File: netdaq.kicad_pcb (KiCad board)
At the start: 2 copper layers, 131.5 x 93 mm, 289 parts, among them J1 RJ45, J3 Conn_01x06_Pin, J4 Micro_SD_Card_Det2, U1 PIC32CK1025GC01100-I/4SB, U10 TLA2518IRTER, U11 TLA2518IRTER, U2 LAN8720A-CP, U5 MP6004GQ-P, U6 PD70100ILD-TR, U7 TPS62A01PDDCR, U8 TLA2518IRTER, U9 TLA2518IRTER, Y4 Crystal_GND24

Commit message: lots
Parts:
- removed TR2: Wuerth_750343373, Transformer_THT:Transformer_Wuerth_750343373
- added C102: 910p, Capacitor_SMD:C_0402_1005Metric, F.Cu at (183.6, 68.5)
- added C103: 22u 10 V, Capacitor_SMD:C_0805_2012Metric, F.Cu at (178.8, 87.2)
- added C104: 22u 10 V, Capacitor_SMD:C_0805_2012Metric, F.Cu at (176.2, 87.2)
- added C105: 220u, Capacitor_SMD:C_Elec_6.3x7.7, F.Cu at (171.2, 87.2)
- added C106: 2.2u 100 V, Capacitor_SMD:C_1206_3216Metric, F.Cu at (180.6, 59.2)
- added C107: 1u 10V, Capacitor_SMD:C_0402_1005Metric, F.Cu at (177.6, 64.0)
- added C108: C, Capacitor_SMD:C_0402_1005Metric, F.Cu at (185.2, 82.8)
- added C134: 47u, Capacitor_SMD:C_Elec_10x10.2, F.Cu at (171.2, 63.8)
- added C135: 100n 100V, Capacitor_SMD:C_0603_1608Metric, F.Cu at (165.5, 72.3)
- added C136: 4.7u, Capacitor_SMD:C_0805_2012Metric, F.Cu at (168.0, 70.2)
- added D37: US1MFA, Diode_SMD:D_SOD-123F, F.Cu at (180.8, 68.2)
- added D38: VS-10BQ060-M3/5BT, SMB:SMB(DO-214AA), F.Cu at (182.0, 86.2)
- added D39: SMBJ58A, Diode_SMD:D_SMB, F.Cu at (161.0, 60.5)
- added D80: MMBZ5256ELT1G, MMBZ5256ELT1G:SOT-23(1-3), F.Cu at (184.1, 61.2)
- added FB4: FerriteBead, Resistor_SMD:R_0402_1005Metric, F.Cu at (203.3, 76.0)
- added H1: MountingHole, MountingHole:MountingHole_3.2mm_M3_ISO14580, F.Cu at (133.5, 60.0)
- added H2: MountingHole, MountingHole:MountingHole_3.2mm_M3_ISO14580, F.Cu at (206.5, 60.0)
- added H3: MountingHole, MountingHole:MountingHole_3.2mm_M3_ISO14580, F.Cu at (133.5, 135.5)
- added H4: MountingHole, MountingHole:MountingHole_3.2mm_M3_ISO14580, F.Cu at (206.5, 135.5)
- added R100: 240k, Resistor_SMD:R_0402_1005Metric, F.Cu at (172.8, 75.0)
- added R101: 133, Resistor_SMD:R_0402_1005Metric, F.Cu at (172.8, 73.8)
- added R102: 24.9k, Resistor_SMD:R_0402_1005Metric, F.Cu at (165.2, 75.2)
- added R103: 500, Resistor_SMD:R_0603_1608Metric, F.Cu at (185.2, 87.5)
- added R104: 13k, Resistor_SMD:R_0402_1005Metric, F.Cu at (184.1, 65.0)
- added R105: 10k, Resistor_SMD:R_0402_1005Metric, F.Cu at (184.1, 63.7)
- added R106: 330k, Resistor_SMD:R_0402_1005Metric, F.Cu at (177.6, 62.0)
- added R76: 56k, Resistor_SMD:R_0402_1005Metric, F.Cu at (183.6, 66.5)
- added R77: R, Resistor_SMD:R_0402_1005Metric, F.Cu at (185.2, 84.8)
- added R78: 68k, Resistor_SMD:R_0402_1005Metric, F.Cu at (177.6, 68.0)
- added R79: 12k, Resistor_SMD:R_0402_1005Metric, F.Cu at (177.6, 66.0)
- added T2: POE30P-50L, POE30P-50L:POE30P-50L, F.Cu at (179.5, 76.5)
- added U12: PD70100ILD-TR, PD70100ILD-TR:DFN12_4X3_MCH, F.Cu at (169.0, 73.6)
- added USB1: HYCW498-USBC16-735B, C42400252:USB-C-SMD_HYCW498-USBC16-735B, F.Cu at (197.0, 60.0)
- U6: value PD70100ILD-TR -> TPUSBLC6-4SC6; footprint PD70100ILD-TR:DFN12_4X3_MCH -> Package_TO_SOT_SMD:SOT-23-6_Handsoldering
- moved J3 163.1 mm to (205.0, 115.4)
- moved C109 109.4 mm to (192.0, 88.5), turned to 0 degrees
- moved R81 105.6 mm to (188.5, 89.5), turned to 180 degrees
- moved U7 103.1 mm to (190.0, 92.5), turned to 90 degrees
- moved L1 102.8 mm to (194.0, 95.5), turned to -90 degrees
- moved R83 102.5 mm to (187.5, 91.5), turned to 90 degrees
- moved R80 101.4 mm to (186.0, 91.5), turned to -90 degrees
- moved R82 98.2 mm to (187.5, 95.0), turned to -90 degrees
- moved C110 95.8 mm to (190.4, 99.0), turned to 180 degrees
- moved C112 92.9 mm to (190.4, 101.5), turned to 180 degrees
- moved C111 90.1 mm to (190.4, 104.0), turned to 180 degrees
- moved U6 25.9 mm to (198.9, 77.5)
- moved U3 7.64 mm to (160.5, 65.6)
- moved U4 7.63 mm to (160.5, 72.3)
- moved U5 5.52 mm to (180.5, 64.0), turned to 180 degrees
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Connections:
- U5 pad 1: ETH_SHIELD -> PGND
- U5 pad 10: ETH_SHIELD -> PGND
- U5 pad 15: ETH_SHIELD -> PGND
- U5 pad 2: ETH_SHIELD -> PGND
- U5 pad 3: unconnected-(U5-EN-Pad3) -> /PoE Regulator/FLY_EN
- U5 pad 5: /PoE Regulator/VIN -> /Ethernet Connector/POE_V+
- U5 pad 6: /PoE Regulator/VIN -> /Ethernet Connector/POE_V+
- U5 pad 7: unconnected-(U5-MODE-Pad7) -> PGND
- U5 pad 9: unconnected-(U5-ILIM-Pad9) -> Net-(U5-ILIM)
- U6 pad 1: unconnected-(U6-RDET-Pad1) -> /USB.D+
- U6 pad 2: unconnected-(U6-RREF-Pad2) -> GND
- U6 pad 5: unconnected-(U6-VPNIN-Pad5) -> /USB Connector/EXT_VBUS
- U6 pad 6: unconnected-(U6-NC-Pad6) -> /USB.D-
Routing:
- net /Ethernet Connector/POE_V-: track 0.00 -> 27.2 mm
- net PGND: track 0.00 -> 20.2 mm
- net /RMII.TXD1: track 27.6 -> 13.8 mm
- net /RMII.TXD0: track 27.2 -> 14.5 mm
- net /SMI.MDIO: track 47.7 -> 35.5 mm
- net /RMII.TXEN: track 26.9 -> 14.8 mm
- net /SMI.MDC: track 47.8 -> 36.1 mm
- net /RMII.CRSDV: track 26.7 -> 15.1 mm
- net /Ethernet Connector/POE_V+: track 0.00 -> 10.5 mm, vias 0 -> 16
- net /RMII.RXER: track 34.3 -> 24.3 mm
- net +5.0V: track 0.91 -> 8.01 mm
- net /RMII.RXD1: track 43.4 -> 36.5 mm
- net /PoE Regulator/FLY_SW: track 0.00 -> 6.70 mm
- net GND: track 12.2 -> 18.8 mm
- net /PoE Regulator/FLY_FB: track 0.00 -> 6.29 mm, vias 0 -> 2
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- added copper zone on F.Cu, net /Ethernet Connector/POE_CT1
- added copper zone on F.Cu, net /Ethernet Connector/POE_CT2
- added copper zone on B.Cu, net /Ethernet Connector/POE_V+
- added copper zone on F.Cu, net /Ethernet Connector/POE_V+
- added copper zone on F.Cu, net /Ethernet Connector/POE_V-
- added copper zone on F.Cu, net /PD Controller/PD_AUX
- added copper zone on F.Cu, net /PoE Regulator/FLY_SW
- added copper zone on F.Cu, net Net-(D38-A)
- added copper zone on F.Cu, net Net-(R33-Pad1)
- added copper zone on F.Cu, net Net-(R34-Pad1)
- added copper zone on F.Cu, net PGND
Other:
- board size 131.5 x 93 mm -> 80 x 89 mm
- board text removed: "3v3"

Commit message: almost finished usb
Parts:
- added C127: 100n 10V, Capacitor_SMD:C_0402_1005Metric, F.Cu at (194.2, 72.8)
- added C128: 10u 10V, Capacitor_SMD:C_0805_2012Metric, F.Cu at (194.0, 74.5)
- added R92: 5.1k, Resistor_SMD:R_0402_1005Metric, F.Cu at (198.5, 65.5)
- added R93: 5.1k, Resistor_SMD:R_0402_1005Metric, F.Cu at (195.5, 65.5)
- added TP172: TestPoint, TestPoint:TestPoint_THTPad_D1.0mm_Drill0.5mm, F.Cu at (193.0, 67.5)
- added TP173: TestPoint, TestPoint:TestPoint_THTPad_D1.0mm_Drill0.5mm, F.Cu at (204.0, 70.5)
- added TP174: TestPoint, TestPoint:TestPoint_THTPad_D1.0mm_Drill0.5mm, F.Cu at (204.0, 73.0)
- added TP175: TestPoint, TestPoint:TestPoint_THTPad_D1.0mm_Drill0.5mm, F.Cu at (198.5, 71.0)
- added TP176: TestPoint, TestPoint:TestPoint_THTPad_D1.0mm_Drill0.5mm, F.Cu at (195.5, 71.0)
- added TP177: TestPoint_Alt, TestPoint:TestPoint_THTPad_1.0x1.0mm_Drill0.5mm, F.Cu at (201.5, 65.5)
- added TP178: TestPoint, TestPoint:TestPoint_THTPad_D1.0mm_Drill0.5mm, F.Cu at (206.8, 64.5)
- added TP179: TestPoint, TestPoint:TestPoint_THTPad_D1.0mm_Drill0.5mm, F.Cu at (206.8, 66.8)
- added U13: DLM0NSN500HY2D, C913480:FILTER-SMD_4P-L0.8-W0.6-TL_DLP0NSC280HL2L, F.Cu at (197.0, 73.5)
- moved FB4 11.9 mm to (193.0, 70.0), turned to 90 degrees
- moved U6 9.64 mm to (197.0, 68.0), turned to 180 degrees
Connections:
- FB4 pad 1: /USB Connector/VBUS -> +5V_USB
- U6 pad 1: /USB.D+ -> /USB Connector/EXT_USB_D+
- U6 pad 3: unconnected-(U6-Pad3) -> /USB Connector/EXT_USB_CC1
- U6 pad 4: unconnected-(U6-Pad4) -> /USB Connector/EXT_USB_CC2
- U6 pad 6: /USB.D- -> /USB Connector/EXT_USB_D-
- USB1 pad 1: unconnected-(USB1-SHELL-Pad1) -> GND
- USB1 pad 2: (no net) -> GND
- USB1 pad 3: (no net) -> GND
- USB1 pad 4: (no net) -> GND
- USB1 pad A1B12: unconnected-(USB1-GND-PadA1B12) -> GND
- USB1 pad A4B9: unconnected-(USB1-VBUS-PadA4B9) -> /USB Connector/EXT_VBUS
- USB1 pad A5: unconnected-(USB1-CC1-PadA5) -> /USB Connector/EXT_USB_CC1
- USB1 pad A6: unconnected-(USB1-DP1-PadA6) -> /USB Connector/EXT_USB_D+
- USB1 pad A7: unconnected-(USB1-DN1-PadA7) -> /USB Connector/EXT_USB_D-
- USB1 pad A8: unconnected-(USB1-SBU1-PadA8) -> /USB Connector/NC_USB_SBU1
- USB1 pad B1A12: unconnected-(USB1-GND-PadB1A12) -> GND
- USB1 pad B4A9: unconnected-(USB1-VBUS-PadB4A9) -> /USB Connector/EXT_VBUS
- USB1 pad B5: unconnected-(USB1-CC2-PadB5) -> /USB Connector/EXT_USB_CC2
- USB1 pad B6: unconnected-(USB1-DP2-PadB6) -> /USB Connector/EXT_USB_D+
- USB1 pad B7: unconnected-(USB1-DN2-PadB7) -> /USB Connector/EXT_USB_D-
- USB1 pad B8: unconnected-(USB1-SBU2-PadB8) -> /USB Connector/NC_USB_SBU2
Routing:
- net /USB Connector/NC_USB_SBU1: track 0.00 -> 13.6 mm, vias 0 -> 1
- net /USB Connector/NC_USB_SBU2: track 0.00 -> 11.2 mm, vias 0 -> 1
- net /USB Connector/EXT_USB_CC2: track 0.00 -> 5.01 mm
- net /USB Connector/EXT_USB_CC1: track 0.00 -> 4.81 mm
- net GND: track 18.8 -> 21.8 mm

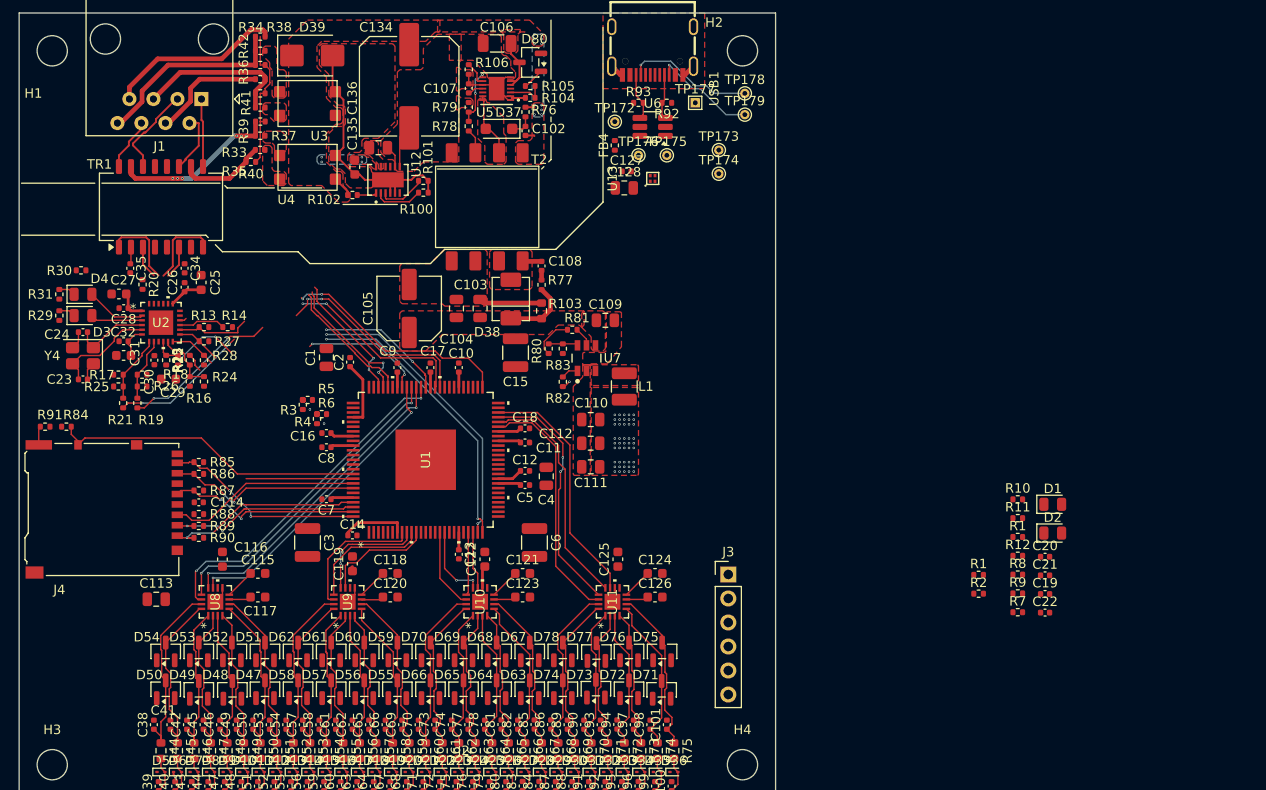
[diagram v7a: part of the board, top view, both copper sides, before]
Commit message: changed to 4 layer, finished usb conn, added jtag conn, some other things
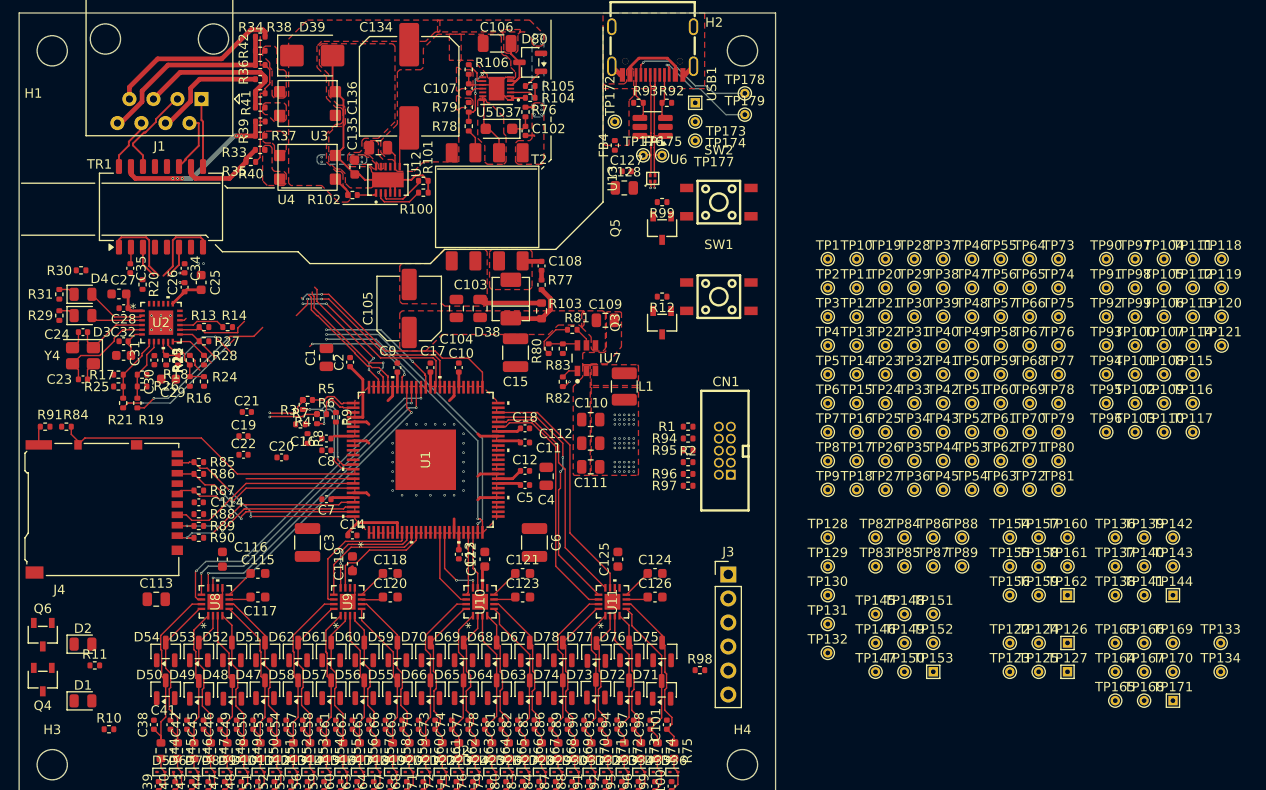
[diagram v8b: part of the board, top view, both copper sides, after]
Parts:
- removed the R1 at (235.6, 111.4)
- added CN1: HX JN1.27-2X5P ZZ H4.9, C42372547:CONN-TH_10P-P1.27_HX-JN1.27-2X5P-ZZ-H4.9, F.Cu at (204.6, 102.3)
- added Q3: BSS138LT1G, C82045:SOT-23-3_L2.9-W1.6-P1.90-LS2.8-BR, F.Cu at (198.0, 88.8)
- added Q4: BSS138LT1G, C82045:SOT-23-3_L2.9-W1.6-P1.90-LS2.8-BR, F.Cu at (132.5, 126.5)
- added Q5: BSS138LT1G, C82045:SOT-23-3_L2.9-W1.6-P1.90-LS2.8-BR, F.Cu at (198.0, 78.8)
- added Q6: BSS138LT1G, C82045:SOT-23-3_L2.9-W1.6-P1.90-LS2.8-BR, F.Cu at (132.5, 121.8)
- added R94: 10k, Resistor_SMD:R_0402_1005Metric, F.Cu at (200.8, 101.0)
- added R95: 10k, Resistor_SMD:R_0402_1005Metric, F.Cu at (200.8, 102.2)
- added R96: 10k, Resistor_SMD:R_0402_1005Metric, F.Cu at (200.8, 104.8)
- added R97: 10k, Resistor_SMD:R_0402_1005Metric, F.Cu at (200.8, 106.0)
- added R98: 10k, Resistor_SMD:R_0402_1005Metric, F.Cu at (202.0, 125.5)
- added R99: 10k, Resistor_SMD:R_0402_1005Metric, F.Cu at (198.0, 76.0)
- added SW1: TS110926043, C22375349:SW-SMD_4P-L4.5-W4.5-P3.00-LS7.5, F.Cu at (204.0, 86.0)
- added SW2: TS110926043, C22375349:SW-SMD_4P-L4.5-W4.5-P3.00-LS7.5, F.Cu at (204.0, 76.0)
- added TP1: TestPoint, TestPoint:TestPoint_THTPad_D1.0mm_Drill0.5mm, F.Cu at (215.5, 82.0)
- added TP10: TestPoint, TestPoint:TestPoint_THTPad_D1.0mm_Drill0.5mm, F.Cu at (218.6, 82.0)
- added TP100: TestPoint, TestPoint:TestPoint_THTPad_D1.0mm_Drill0.5mm, F.Cu at (248.0, 91.2)
- added TP101: TestPoint, TestPoint:TestPoint_THTPad_D1.0mm_Drill0.5mm, F.Cu at (248.0, 94.2)
- added TP102: TestPoint, TestPoint:TestPoint_THTPad_D1.0mm_Drill0.5mm, F.Cu at (248.0, 97.3)
- added TP103: TestPoint, TestPoint:TestPoint_THTPad_D1.0mm_Drill0.5mm, F.Cu at (248.0, 100.3)
- added TP104: TestPoint, TestPoint:TestPoint_THTPad_D1.0mm_Drill0.5mm, F.Cu at (251.1, 82.0)
- added TP105: TestPoint, TestPoint:TestPoint_THTPad_D1.0mm_Drill0.5mm, F.Cu at (251.1, 85.1)
- added TP106: TestPoint, TestPoint:TestPoint_THTPad_D1.0mm_Drill0.5mm, F.Cu at (251.1, 88.1)
- added TP107: TestPoint, TestPoint:TestPoint_THTPad_D1.0mm_Drill0.5mm, F.Cu at (251.1, 91.2)
- added TP108: TestPoint, TestPoint:TestPoint_THTPad_D1.0mm_Drill0.5mm, F.Cu at (251.1, 94.2)
- added TP109: TestPoint, TestPoint:TestPoint_THTPad_D1.0mm_Drill0.5mm, F.Cu at (251.1, 97.3)
- added TP11: TestPoint, TestPoint:TestPoint_THTPad_D1.0mm_Drill0.5mm, F.Cu at (218.6, 85.1)
- added TP110: TestPoint, TestPoint:TestPoint_THTPad_D1.0mm_Drill0.5mm, F.Cu at (251.1, 100.3)
- added TP111: TestPoint, TestPoint:TestPoint_THTPad_D1.0mm_Drill0.5mm, F.Cu at (254.1, 82.0)
- added TP112: TestPoint, TestPoint:TestPoint_THTPad_D1.0mm_Drill0.5mm, F.Cu at (254.1, 85.1)
- added TP113: TestPoint, TestPoint:TestPoint_THTPad_D1.0mm_Drill0.5mm, F.Cu at (254.1, 88.1)
- added TP114: TestPoint, TestPoint:TestPoint_THTPad_D1.0mm_Drill0.5mm, F.Cu at (254.1, 91.2)
- added TP115: TestPoint, TestPoint:TestPoint_THTPad_D1.0mm_Drill0.5mm, F.Cu at (254.1, 94.2)
- added TP116: TestPoint, TestPoint:TestPoint_THTPad_D1.0mm_Drill0.5mm, F.Cu at (254.1, 97.3)
- added TP117: TestPoint, TestPoint:TestPoint_THTPad_D1.0mm_Drill0.5mm, F.Cu at (254.1, 100.3)
- added TP118: TestPoint, TestPoint:TestPoint_THTPad_D1.0mm_Drill0.5mm, F.Cu at (257.2, 82.0)
- added TP119: TestPoint, TestPoint:TestPoint_THTPad_D1.0mm_Drill0.5mm, F.Cu at (257.2, 85.1)
- added TP12: TestPoint, TestPoint:TestPoint_THTPad_D1.0mm_Drill0.5mm, F.Cu at (218.6, 88.1)
- added TP120: TestPoint, TestPoint:TestPoint_THTPad_D1.0mm_Drill0.5mm, F.Cu at (257.2, 88.1)
- added TP121: TestPoint, TestPoint:TestPoint_THTPad_D1.0mm_Drill0.5mm, F.Cu at (257.2, 91.2)
- added TP122: TestPoint, TestPoint:TestPoint_THTPad_D1.0mm_Drill0.5mm, F.Cu at (234.8, 122.6)
- added TP123: TestPoint, TestPoint:TestPoint_THTPad_D1.0mm_Drill0.5mm, F.Cu at (234.8, 125.7)
- added TP124: TestPoint, TestPoint:TestPoint_THTPad_D1.0mm_Drill0.5mm, F.Cu at (237.8, 122.6)
- added TP125: TestPoint, TestPoint:TestPoint_THTPad_D1.0mm_Drill0.5mm, F.Cu at (237.8, 125.7)
- added TP126: TestPoint_Alt, TestPoint:TestPoint_THTPad_1.0x1.0mm_Drill0.5mm, F.Cu at (240.9, 122.6)
- added TP127: TestPoint_Alt, TestPoint:TestPoint_THTPad_1.0x1.0mm_Drill0.5mm, F.Cu at (240.9, 125.7)
- added TP128: TestPoint, TestPoint:TestPoint_THTPad_D1.0mm_Drill0.5mm, F.Cu at (215.5, 111.5)
- added TP129: TestPoint, TestPoint:TestPoint_THTPad_D1.0mm_Drill0.5mm, F.Cu at (215.5, 114.5)
- added TP13: TestPoint, TestPoint:TestPoint_THTPad_D1.0mm_Drill0.5mm, F.Cu at (218.6, 91.2)
- added TP130: TestPoint, TestPoint:TestPoint_THTPad_D1.0mm_Drill0.5mm, F.Cu at (215.5, 117.6)
- added TP131: TestPoint, TestPoint:TestPoint_THTPad_D1.0mm_Drill0.5mm, F.Cu at (215.5, 120.6)
- added TP132: TestPoint, TestPoint:TestPoint_THTPad_D1.0mm_Drill0.5mm, F.Cu at (215.5, 123.7)
- added TP133: TestPoint, TestPoint:TestPoint_THTPad_D1.0mm_Drill0.5mm, F.Cu at (257.1, 122.6)
- added TP134: TestPoint, TestPoint:TestPoint_THTPad_D1.0mm_Drill0.5mm, F.Cu at (257.1, 125.7)
- added TP136: TestPoint, TestPoint:TestPoint_THTPad_D1.0mm_Drill0.5mm, F.Cu at (245.9, 111.5)
- added TP137: TestPoint, TestPoint:TestPoint_THTPad_D1.0mm_Drill0.5mm, F.Cu at (245.9, 114.5)
- added TP138: TestPoint, TestPoint:TestPoint_THTPad_D1.0mm_Drill0.5mm, F.Cu at (245.9, 117.6)
- added TP139: TestPoint, TestPoint:TestPoint_THTPad_D1.0mm_Drill0.5mm, F.Cu at (249.0, 111.5)
- added TP14: TestPoint, TestPoint:TestPoint_THTPad_D1.0mm_Drill0.5mm, F.Cu at (218.6, 94.2)
- added TP140: TestPoint, TestPoint:TestPoint_THTPad_D1.0mm_Drill0.5mm, F.Cu at (249.0, 114.5)
- added TP141: TestPoint, TestPoint:TestPoint_THTPad_D1.0mm_Drill0.5mm, F.Cu at (249.0, 117.6)
- added TP142: TestPoint, TestPoint:TestPoint_THTPad_D1.0mm_Drill0.5mm, F.Cu at (252.0, 111.5)
- added TP143: TestPoint, TestPoint:TestPoint_THTPad_D1.0mm_Drill0.5mm, F.Cu at (252.0, 114.5)
- added TP144: TestPoint_Alt, TestPoint:TestPoint_THTPad_1.0x1.0mm_Drill0.5mm, F.Cu at (252.0, 117.6)
- added TP145: TestPoint, TestPoint:TestPoint_THTPad_D1.0mm_Drill0.5mm, F.Cu at (220.6, 119.6)
- added TP146: TestPoint, TestPoint:TestPoint_THTPad_D1.0mm_Drill0.5mm, F.Cu at (220.6, 122.6)
- added TP147: TestPoint, TestPoint:TestPoint_THTPad_D1.0mm_Drill0.5mm, F.Cu at (220.6, 125.7)
- added TP148: TestPoint, TestPoint:TestPoint_THTPad_D1.0mm_Drill0.5mm, F.Cu at (223.6, 119.6)
- added TP149: TestPoint, TestPoint:TestPoint_THTPad_D1.0mm_Drill0.5mm, F.Cu at (223.6, 122.6)
- added TP15: TestPoint, TestPoint:TestPoint_THTPad_D1.0mm_Drill0.5mm, F.Cu at (218.6, 97.3)
- added TP150: TestPoint, TestPoint:TestPoint_THTPad_D1.0mm_Drill0.5mm, F.Cu at (223.6, 125.7)
- added TP151: TestPoint, TestPoint:TestPoint_THTPad_D1.0mm_Drill0.5mm, F.Cu at (226.7, 119.6)
- added TP152: TestPoint, TestPoint:TestPoint_THTPad_D1.0mm_Drill0.5mm, F.Cu at (226.7, 122.6)
- added TP153: TestPoint_Alt, TestPoint:TestPoint_THTPad_1.0x1.0mm_Drill0.5mm, F.Cu at (226.7, 125.7)
- added TP154: TestPoint, TestPoint:TestPoint_THTPad_D1.0mm_Drill0.5mm, F.Cu at (234.8, 111.5)
- added TP155: TestPoint, TestPoint:TestPoint_THTPad_D1.0mm_Drill0.5mm, F.Cu at (234.8, 114.5)
- added TP156: TestPoint, TestPoint:TestPoint_THTPad_D1.0mm_Drill0.5mm, F.Cu at (234.8, 117.6)
- added TP157: TestPoint, TestPoint:TestPoint_THTPad_D1.0mm_Drill0.5mm, F.Cu at (237.8, 111.5)
- added TP158: TestPoint, TestPoint:TestPoint_THTPad_D1.0mm_Drill0.5mm, F.Cu at (237.8, 114.5)
- added TP159: TestPoint, TestPoint:TestPoint_THTPad_D1.0mm_Drill0.5mm, F.Cu at (237.8, 117.6)
- added TP16: TestPoint, TestPoint:TestPoint_THTPad_D1.0mm_Drill0.5mm, F.Cu at (218.6, 100.3)
- added TP160: TestPoint, TestPoint:TestPoint_THTPad_D1.0mm_Drill0.5mm, F.Cu at (240.9, 111.5)
- added TP161: TestPoint, TestPoint:TestPoint_THTPad_D1.0mm_Drill0.5mm, F.Cu at (240.9, 114.5)
- added TP162: TestPoint_Alt, TestPoint:TestPoint_THTPad_1.0x1.0mm_Drill0.5mm, F.Cu at (240.9, 117.6)
- added TP163: TestPoint, TestPoint:TestPoint_THTPad_D1.0mm_Drill0.5mm, F.Cu at (245.9, 122.6)
- added TP164: TestPoint, TestPoint:TestPoint_THTPad_D1.0mm_Drill0.5mm, F.Cu at (245.9, 125.7)
- added TP165: TestPoint, TestPoint:TestPoint_THTPad_D1.0mm_Drill0.5mm, F.Cu at (245.9, 128.7)
- added TP166: TestPoint, TestPoint:TestPoint_THTPad_D1.0mm_Drill0.5mm, F.Cu at (249.0, 122.6)
- added TP167: TestPoint, TestPoint:TestPoint_THTPad_D1.0mm_Drill0.5mm, F.Cu at (249.0, 125.7)
- added TP168: TestPoint, TestPoint:TestPoint_THTPad_D1.0mm_Drill0.5mm, F.Cu at (249.0, 128.7)
- added TP169: TestPoint, TestPoint:TestPoint_THTPad_D1.0mm_Drill0.5mm, F.Cu at (252.0, 122.6)
- added TP17: TestPoint, TestPoint:TestPoint_THTPad_D1.0mm_Drill0.5mm, F.Cu at (218.6, 103.4)
- added TP170: TestPoint, TestPoint:TestPoint_THTPad_D1.0mm_Drill0.5mm, F.Cu at (252.0, 125.7)
- added TP171: TestPoint_Alt, TestPoint:TestPoint_THTPad_1.0x1.0mm_Drill0.5mm, F.Cu at (252.0, 128.7)
- added TP18: TestPoint, TestPoint:TestPoint_THTPad_D1.0mm_Drill0.5mm, F.Cu at (218.6, 106.4)
- added TP19: TestPoint, TestPoint:TestPoint_THTPad_D1.0mm_Drill0.5mm, F.Cu at (221.6, 82.0)
- added TP2: TestPoint, TestPoint:TestPoint_THTPad_D1.0mm_Drill0.5mm, F.Cu at (215.5, 85.1)
- added TP20: TestPoint, TestPoint:TestPoint_THTPad_D1.0mm_Drill0.5mm, F.Cu at (221.6, 85.1)
- added TP21: TestPoint, TestPoint:TestPoint_THTPad_D1.0mm_Drill0.5mm, F.Cu at (221.6, 88.1)
- added TP22: TestPoint, TestPoint:TestPoint_THTPad_D1.0mm_Drill0.5mm, F.Cu at (221.6, 91.2)
- added TP23: TestPoint, TestPoint:TestPoint_THTPad_D1.0mm_Drill0.5mm, F.Cu at (221.6, 94.2)
- added TP24: TestPoint, TestPoint:TestPoint_THTPad_D1.0mm_Drill0.5mm, F.Cu at (221.6, 97.3)
- added TP25: TestPoint, TestPoint:TestPoint_THTPad_D1.0mm_Drill0.5mm, F.Cu at (221.6, 100.3)
- added TP26: TestPoint, TestPoint:TestPoint_THTPad_D1.0mm_Drill0.5mm, F.Cu at (221.6, 103.4)
- added TP27: TestPoint, TestPoint:TestPoint_THTPad_D1.0mm_Drill0.5mm, F.Cu at (221.6, 106.4)
- added TP28: TestPoint, TestPoint:TestPoint_THTPad_D1.0mm_Drill0.5mm, F.Cu at (224.7, 82.0)
- added TP29: TestPoint, TestPoint:TestPoint_THTPad_D1.0mm_Drill0.5mm, F.Cu at (224.7, 85.1)
- added TP3: TestPoint, TestPoint:TestPoint_THTPad_D1.0mm_Drill0.5mm, F.Cu at (215.5, 88.1)
- added TP30: TestPoint, TestPoint:TestPoint_THTPad_D1.0mm_Drill0.5mm, F.Cu at (224.7, 88.1)
- added TP31: TestPoint, TestPoint:TestPoint_THTPad_D1.0mm_Drill0.5mm, F.Cu at (224.7, 91.2)
- added TP32: TestPoint, TestPoint:TestPoint_THTPad_D1.0mm_Drill0.5mm, F.Cu at (224.7, 94.2)
- added TP33: TestPoint, TestPoint:TestPoint_THTPad_D1.0mm_Drill0.5mm, F.Cu at (224.7, 97.3)
- added TP34: TestPoint, TestPoint:TestPoint_THTPad_D1.0mm_Drill0.5mm, F.Cu at (224.7, 100.3)
- added TP35: TestPoint, TestPoint:TestPoint_THTPad_D1.0mm_Drill0.5mm, F.Cu at (224.7, 103.4)
- added TP36: TestPoint, TestPoint:TestPoint_THTPad_D1.0mm_Drill0.5mm, F.Cu at (224.7, 106.4)
- added TP37: TestPoint, TestPoint:TestPoint_THTPad_D1.0mm_Drill0.5mm, F.Cu at (227.7, 82.0)
- added TP38: TestPoint, TestPoint:TestPoint_THTPad_D1.0mm_Drill0.5mm, F.Cu at (227.7, 85.1)
- added TP39: TestPoint, TestPoint:TestPoint_THTPad_D1.0mm_Drill0.5mm, F.Cu at (227.7, 88.1)
- added TP4: TestPoint, TestPoint:TestPoint_THTPad_D1.0mm_Drill0.5mm, F.Cu at (215.5, 91.2)
- added TP40: TestPoint, TestPoint:TestPoint_THTPad_D1.0mm_Drill0.5mm, F.Cu at (227.7, 91.2)
- added TP41: TestPoint, TestPoint:TestPoint_THTPad_D1.0mm_Drill0.5mm, F.Cu at (227.7, 94.2)
- added TP42: TestPoint, TestPoint:TestPoint_THTPad_D1.0mm_Drill0.5mm, F.Cu at (227.7, 97.3)
- added TP43: TestPoint, TestPoint:TestPoint_THTPad_D1.0mm_Drill0.5mm, F.Cu at (227.7, 100.3)
- added TP44: TestPoint, TestPoint:TestPoint_THTPad_D1.0mm_Drill0.5mm, F.Cu at (227.7, 103.4)
- added TP45: TestPoint, TestPoint:TestPoint_THTPad_D1.0mm_Drill0.5mm, F.Cu at (227.7, 106.4)
- added TP46: TestPoint, TestPoint:TestPoint_THTPad_D1.0mm_Drill0.5mm, F.Cu at (230.8, 82.0)
- added TP47: TestPoint, TestPoint:TestPoint_THTPad_D1.0mm_Drill0.5mm, F.Cu at (230.8, 85.1)
- added TP48: TestPoint, TestPoint:TestPoint_THTPad_D1.0mm_Drill0.5mm, F.Cu at (230.8, 88.1)
- added TP49: TestPoint, TestPoint:TestPoint_THTPad_D1.0mm_Drill0.5mm, F.Cu at (230.8, 91.2)
- added TP5: TestPoint, TestPoint:TestPoint_THTPad_D1.0mm_Drill0.5mm, F.Cu at (215.5, 94.2)
- added TP50: TestPoint, TestPoint:TestPoint_THTPad_D1.0mm_Drill0.5mm, F.Cu at (230.8, 94.2)
- added TP51: TestPoint, TestPoint:TestPoint_THTPad_D1.0mm_Drill0.5mm, F.Cu at (230.8, 97.3)
- added TP52: TestPoint, TestPoint:TestPoint_THTPad_D1.0mm_Drill0.5mm, F.Cu at (230.8, 100.3)
- added TP53: TestPoint, TestPoint:TestPoint_THTPad_D1.0mm_Drill0.5mm, F.Cu at (230.8, 103.4)
- added TP54: TestPoint, TestPoint:TestPoint_THTPad_D1.0mm_Drill0.5mm, F.Cu at (230.8, 106.4)
- added TP55: TestPoint, TestPoint:TestPoint_THTPad_D1.0mm_Drill0.5mm, F.Cu at (233.8, 82.0)
- added TP56: TestPoint, TestPoint:TestPoint_THTPad_D1.0mm_Drill0.5mm, F.Cu at (233.8, 85.1)
- added TP57: TestPoint, TestPoint:TestPoint_THTPad_D1.0mm_Drill0.5mm, F.Cu at (233.8, 88.1)
- added TP58: TestPoint, TestPoint:TestPoint_THTPad_D1.0mm_Drill0.5mm, F.Cu at (233.8, 91.2)
- added TP59: TestPoint, TestPoint:TestPoint_THTPad_D1.0mm_Drill0.5mm, F.Cu at (233.8, 94.2)
- added TP6: TestPoint, TestPoint:TestPoint_THTPad_D1.0mm_Drill0.5mm, F.Cu at (215.5, 97.3)
- added TP60: TestPoint, TestPoint:TestPoint_THTPad_D1.0mm_Drill0.5mm, F.Cu at (233.8, 97.3)
- added TP61: TestPoint, TestPoint:TestPoint_THTPad_D1.0mm_Drill0.5mm, F.Cu at (233.8, 100.3)
- added TP62: TestPoint, TestPoint:TestPoint_THTPad_D1.0mm_Drill0.5mm, F.Cu at (233.8, 103.4)
- added TP63: TestPoint, TestPoint:TestPoint_THTPad_D1.0mm_Drill0.5mm, F.Cu at (233.8, 106.4)
- added TP64: TestPoint, TestPoint:TestPoint_THTPad_D1.0mm_Drill0.5mm, F.Cu at (236.9, 82.0)
- added TP65: TestPoint, TestPoint:TestPoint_THTPad_D1.0mm_Drill0.5mm, F.Cu at (236.9, 85.1)
- added TP66: TestPoint, TestPoint:TestPoint_THTPad_D1.0mm_Drill0.5mm, F.Cu at (236.9, 88.1)
- added TP67: TestPoint, TestPoint:TestPoint_THTPad_D1.0mm_Drill0.5mm, F.Cu at (236.9, 91.2)
- added TP68: TestPoint, TestPoint:TestPoint_THTPad_D1.0mm_Drill0.5mm, F.Cu at (236.9, 94.2)
- added TP69: TestPoint, TestPoint:TestPoint_THTPad_D1.0mm_Drill0.5mm, F.Cu at (236.9, 97.3)
- added TP7: TestPoint, TestPoint:TestPoint_THTPad_D1.0mm_Drill0.5mm, F.Cu at (215.5, 100.3)
- added TP70: TestPoint, TestPoint:TestPoint_THTPad_D1.0mm_Drill0.5mm, F.Cu at (236.9, 100.3)
- added TP71: TestPoint, TestPoint:TestPoint_THTPad_D1.0mm_Drill0.5mm, F.Cu at (236.9, 103.4)
- added TP72: TestPoint, TestPoint:TestPoint_THTPad_D1.0mm_Drill0.5mm, F.Cu at (236.9, 106.4)
- added TP73: TestPoint, TestPoint:TestPoint_THTPad_D1.0mm_Drill0.5mm, F.Cu at (239.9, 82.0)
- added TP74: TestPoint, TestPoint:TestPoint_THTPad_D1.0mm_Drill0.5mm, F.Cu at (239.9, 85.1)
- added TP75: TestPoint, TestPoint:TestPoint_THTPad_D1.0mm_Drill0.5mm, F.Cu at (239.9, 88.1)
- added TP76: TestPoint, TestPoint:TestPoint_THTPad_D1.0mm_Drill0.5mm, F.Cu at (239.9, 91.2)
- added TP77: TestPoint, TestPoint:TestPoint_THTPad_D1.0mm_Drill0.5mm, F.Cu at (239.9, 94.2)
- added TP78: TestPoint, TestPoint:TestPoint_THTPad_D1.0mm_Drill0.5mm, F.Cu at (239.9, 97.3)
- added TP79: TestPoint, TestPoint:TestPoint_THTPad_D1.0mm_Drill0.5mm, F.Cu at (239.9, 100.3)
- added TP8: TestPoint, TestPoint:TestPoint_THTPad_D1.0mm_Drill0.5mm, F.Cu at (215.5, 103.4)
- added TP80: TestPoint, TestPoint:TestPoint_THTPad_D1.0mm_Drill0.5mm, F.Cu at (239.9, 103.4)
- added TP81: TestPoint, TestPoint:TestPoint_THTPad_D1.0mm_Drill0.5mm, F.Cu at (239.9, 106.4)
- added TP82: TestPoint, TestPoint:TestPoint_THTPad_D1.0mm_Drill0.5mm, F.Cu at (220.6, 111.5)
- added TP83: TestPoint, TestPoint:TestPoint_THTPad_D1.0mm_Drill0.5mm, F.Cu at (220.6, 114.5)
- added TP84: TestPoint, TestPoint:TestPoint_THTPad_D1.0mm_Drill0.5mm, F.Cu at (223.6, 111.5)
- added TP85: TestPoint, TestPoint:TestPoint_THTPad_D1.0mm_Drill0.5mm, F.Cu at (223.6, 114.5)
- added TP86: TestPoint, TestPoint:TestPoint_THTPad_D1.0mm_Drill0.5mm, F.Cu at (226.7, 111.5)
- added TP87: TestPoint, TestPoint:TestPoint_THTPad_D1.0mm_Drill0.5mm, F.Cu at (226.7, 114.5)
- added TP88: TestPoint, TestPoint:TestPoint_THTPad_D1.0mm_Drill0.5mm, F.Cu at (229.7, 111.5)
- added TP89: TestPoint, TestPoint:TestPoint_THTPad_D1.0mm_Drill0.5mm, F.Cu at (229.7, 114.5)
- added TP9: TestPoint, TestPoint:TestPoint_THTPad_D1.0mm_Drill0.5mm, F.Cu at (215.5, 106.4)
- added TP90: TestPoint, TestPoint:TestPoint_THTPad_D1.0mm_Drill0.5mm, F.Cu at (245.0, 82.0)
- added TP91: TestPoint, TestPoint:TestPoint_THTPad_D1.0mm_Drill0.5mm, F.Cu at (245.0, 85.1)
- added TP92: TestPoint, TestPoint:TestPoint_THTPad_D1.0mm_Drill0.5mm, F.Cu at (245.0, 88.1)
- added TP93: TestPoint, TestPoint:TestPoint_THTPad_D1.0mm_Drill0.5mm, F.Cu at (245.0, 91.2)
- added TP94: TestPoint, TestPoint:TestPoint_THTPad_D1.0mm_Drill0.5mm, F.Cu at (245.0, 94.2)
- added TP95: TestPoint, TestPoint:TestPoint_THTPad_D1.0mm_Drill0.5mm, F.Cu at (245.0, 97.3)
- added TP96: TestPoint, TestPoint:TestPoint_THTPad_D1.0mm_Drill0.5mm, F.Cu at (245.0, 100.3)
- added TP97: TestPoint, TestPoint:TestPoint_THTPad_D1.0mm_Drill0.5mm, F.Cu at (248.0, 82.0)
- added TP98: TestPoint, TestPoint:TestPoint_THTPad_D1.0mm_Drill0.5mm, F.Cu at (248.0, 85.1)
- added TP99: TestPoint, TestPoint:TestPoint_THTPad_D1.0mm_Drill0.5mm, F.Cu at (248.0, 88.1)
- moved D1 104.6 mm to (136.8, 128.8)
- moved D2 103.2 mm to (136.8, 122.8)
- moved R10 99.1 mm to (139.5, 131.8)
- moved R11 98.8 mm to (138.0, 125.0)
- moved C19 86.4 mm to (153.7, 100.8)
- moved C22 86.4 mm to (153.7, 102.7)
- moved C21 86.2 mm to (154.1, 98.2)
- moved C20 81.4 mm to (157.8, 103.0)
- moved R7 78.4 mm to (159.8, 99.5)
- moved R8 76.5 mm to (160.5, 101.0), turned to -90 degrees
- moved R9 74.5 mm to (163.5, 98.8), turned to -90 degrees
- moved R12 46.5 mm to (198.0, 86.0), turned to 180 degrees
- moved R1 34.5 mm to (200.8, 99.8)
- moved R2 33.7 mm to (200.8, 103.5)
- moved TP174 4.30 mm to (201.5, 69.5)
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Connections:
- net /MCU/RESET# renamed /MCU_RST#
- D2 pad 1: GND -> Net-(D2-K)
- R2 pad 2: /MCU/JTAG.TDO -> /JTAG.TDO
- U1 pad 1: /MCU/JTAG.TDI -> /JTAG.TDI
- U1 pad 3: /MCU/JTAG.TMS -> /JTAG.TMS
- U1 pad 4: /MCU/JTAG.TCK -> /JTAG.TCK
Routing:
- net /USB.D+: track 0.00 -> 62.8 mm, vias 0 -> 2
- net /USB.D-: track 0.00 -> 61.7 mm, vias 0 -> 2
- net GND: track 21.8 -> 39.7 mm, vias 1 -> 35
- net /USB Connector/EXT_USB_D-: track 0.00 -> 12.7 mm
- net /USB Connector/EXT_USB_D+: track 0.00 -> 12.7 mm
- net /MCU/USB_FS.D-: track 0.01 -> 11.1 mm, vias 1 -> 2
- net /MCU/USB_FS.D+: track 0.01 -> 10.8 mm, vias 1 -> 2
- net /USB Connector/EXT_VBUS: track 0.00 -> 7.29 mm
- net /MCU/USB_HS.D-: track 0.00 -> 4.79 mm
- net /MCU/USB_HS.D+: track 0.00 -> 4.51 mm
- net +3.3V: track 39.9 -> 37.0 mm
- added copper zone on F.Cu, net /USB Connector/EXT_VBUS
- added copper zone on In2.Cu, net GND
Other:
- copper layers 2 -> 4
